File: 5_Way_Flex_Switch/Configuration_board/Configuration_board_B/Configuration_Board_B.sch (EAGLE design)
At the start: 4 parts

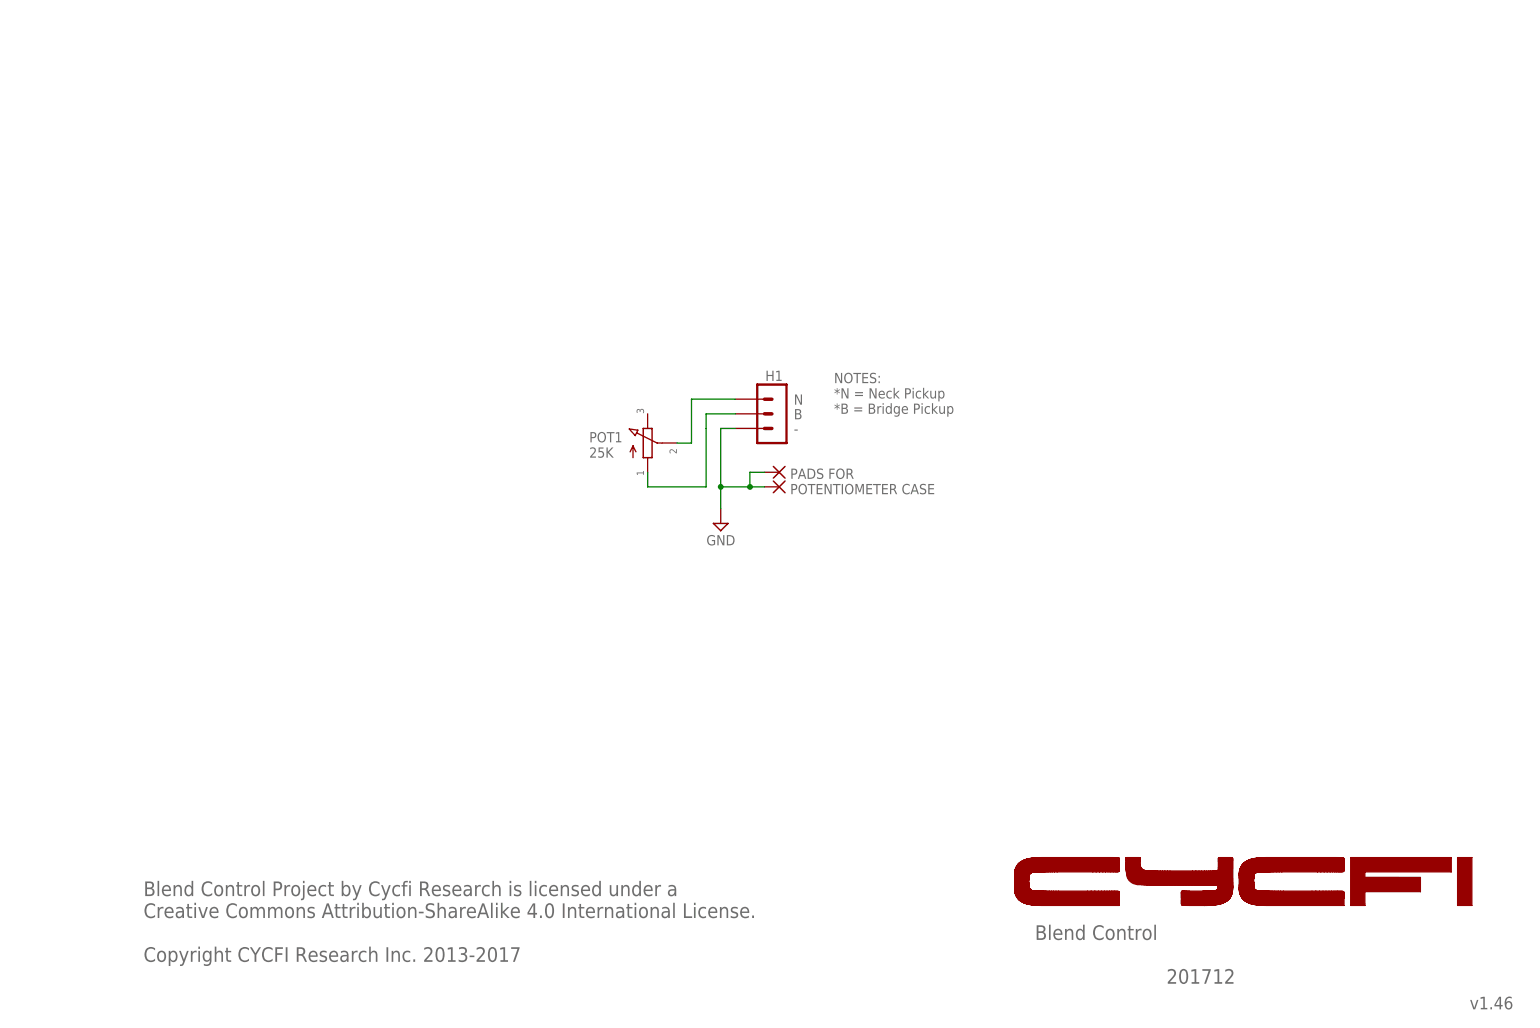
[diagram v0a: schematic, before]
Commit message: *organize 5-waay switch and its configuration board(a and b) *update license date *remove red frame schem pdf files, change with black frame *update document number
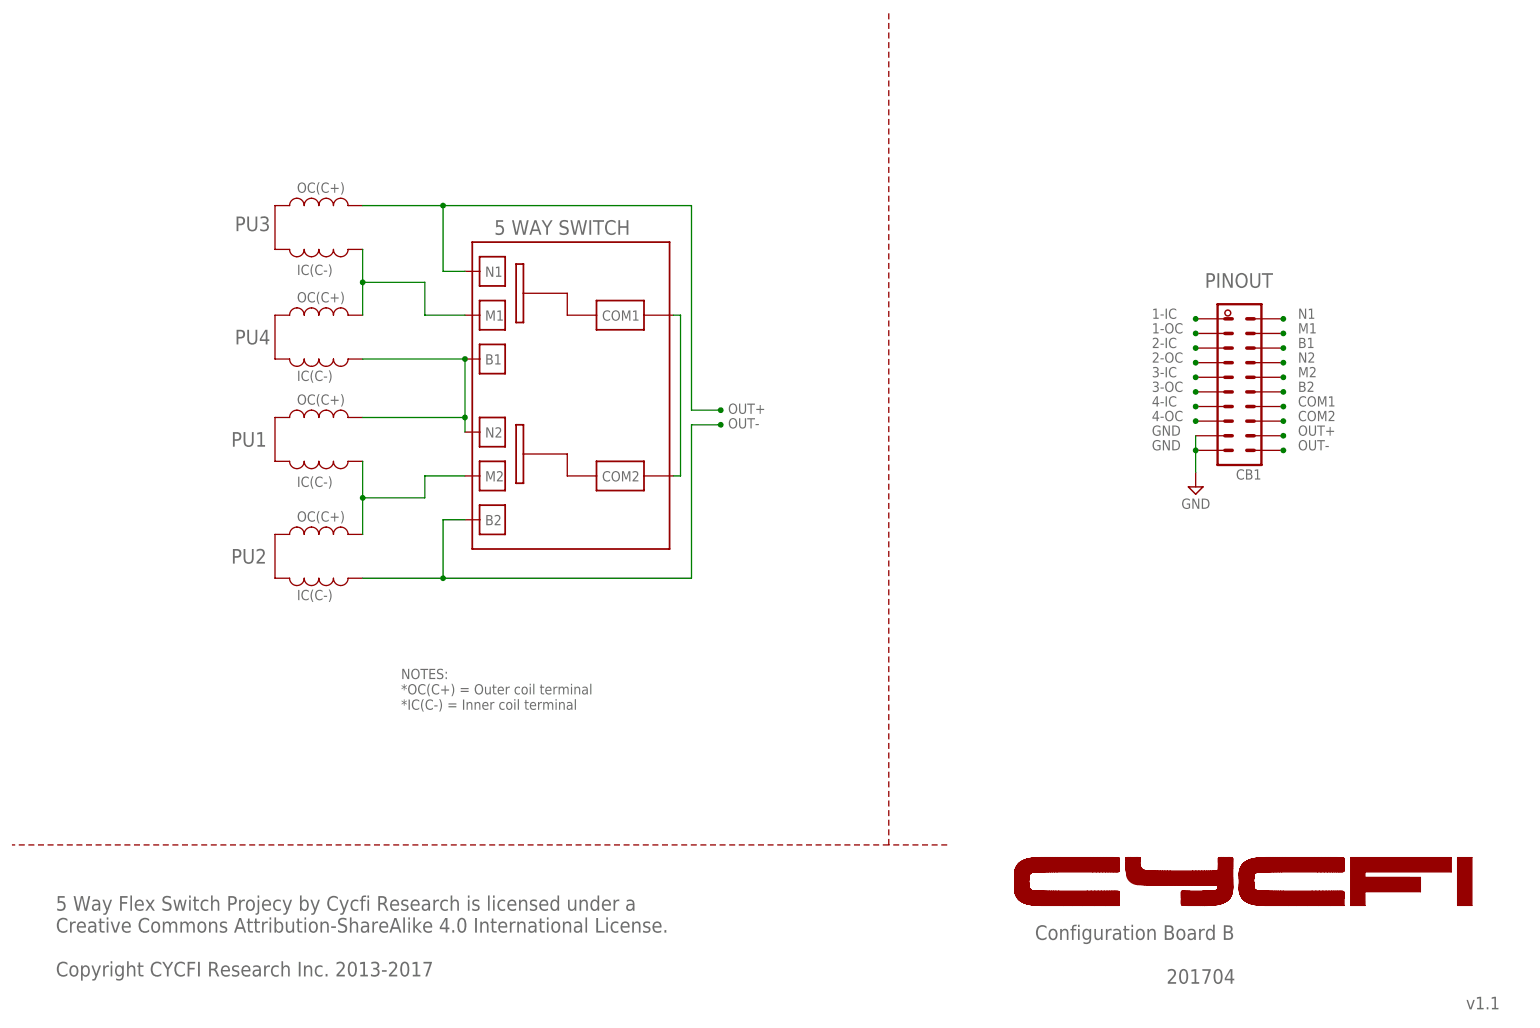
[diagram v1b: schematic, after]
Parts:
- removed GND3, GND4: (no value), wirepad:SMD2
- removed H1: 3PIN-SMD-2.54MM, CYCFI_Con:3PIN-SMD-2.54MM
- removed POT1: PDB181-GTR01, CYCFI_Passive:PDB181-GTR01
- added CB1: CONFIGURATION_BRD_CAST, CYCFI_Module_castellated:CONFIGURATION_BRD_CAST
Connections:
- removed net N$1: H1.3, POT1.2
- removed net N$3: H1.2, POT1.1
- new net 1: CB1.3-OC, CB1.N1, CB1.OUT+
- new net 2: CB1.3-IC, CB1.4-OC, CB1.M1
- new net 3: CB1.1-OC, CB1.4-IC, CB1.B1, CB1.N2
- new net 4: CB1.COM1, CB1.COM2
- new net 5: CB1.1-IC, CB1.2-OC, CB1.M2
- new net 6: CB1.2-IC, CB1.B2, CB1.OUT-
- net GND: now also CB1.GND, CB1.GND1; no longer GND3.P, GND4.P, H1.1
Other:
- note added: "1-IC"
- note added: "1-OC"
- note added: "2-IC"
- note added: "2-OC"
- note added: "201704"
- note added: "3-IC"
- note added: "3-OC"
- note added: "4-IC"
- note added: "4-OC"
- note added: "5 WAY SWITCH"
- note added: "5 Way Flex Switch Projecy by Cycfi Research is licensed under a Creative Commons Attribution-ShareAlike 4.0 International License. Copyright CYCFI Research Inc. 2013-2017"
- note added: "B1"
- note added: "B2"
- note added: "COM1"
- note added: "COM2"
- note added: "Configuration Board B"
- note added: "GND"
- note added: "IC(C-)"
- note added: "M1"
- note added: "M2"
- note added: "N1"
- note added: "N2"
- note added: "NOTES: *OC(C+) = Outer coil terminal *IC(C-) = Inner coil terminal"
- note added: "OC(C+)"
- note added: "OUT+"
- note added: "OUT-"
- note added: "PINOUT"
- note added: "PU1"
- note added: "PU2"
- note added: "PU3"
- note added: "PU4"
- note added: "v1.1"
- note removed: "-"
- note removed: "201712"
- note removed: "B"
- note removed: "Blend Control"
- note removed: "Blend Control Project by Cycfi Research is licensed under a Creative Commons Attribution-ShareAlike 4.0 International License. Copyright CYCFI Research Inc. 2013-2017"
- note removed: "N"
- note removed: "NOTES: *N = Neck Pickup *B = Bridge Pickup"
- note removed: "PADS FOR POTENTIOMETER CASE"
- note removed: "POT1 25K"
- note removed: "v1.46"

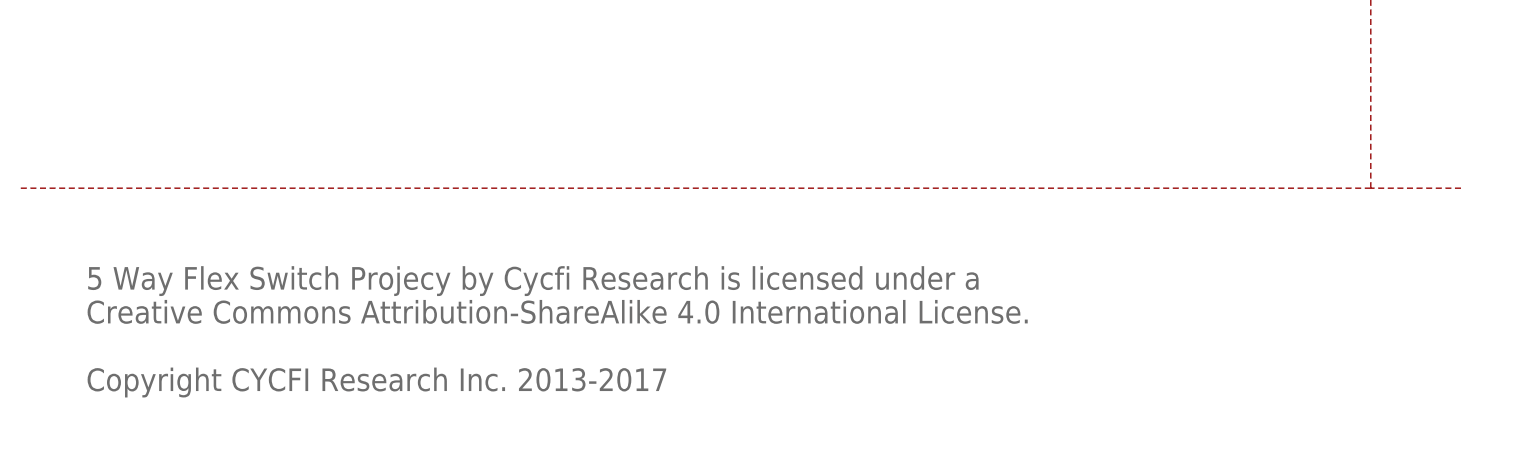
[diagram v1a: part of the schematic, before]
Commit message: Updated broken .sch files
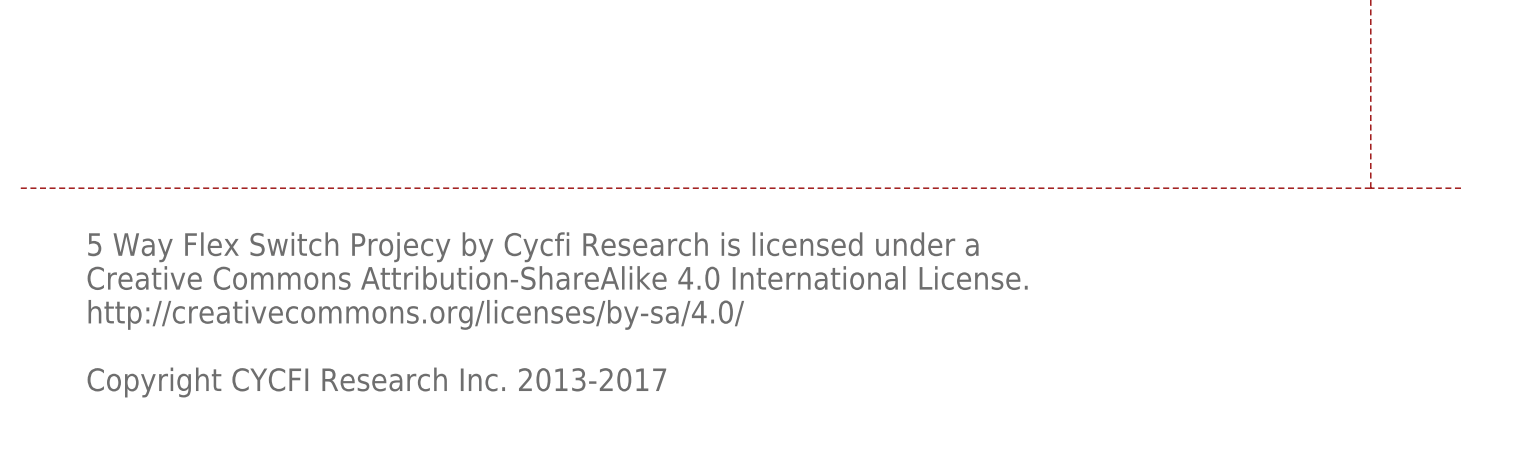
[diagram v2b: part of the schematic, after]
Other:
- note added: "5 Way Flex Switch Projecy by Cycfi Research is licensed under a Creative Commons Attribution-ShareAlike 4.0 International License. http://creativecommons.org/licenses/by-sa/4.0/ Copyright CYCFI Research Inc. 2013-2017"
- note removed: "5 Way Flex Switch Projecy by Cycfi Research is licensed under a Creative Commons Attribution-ShareAlike 4.0 International License. Copyright CYCFI Research Inc. 2013-2017"
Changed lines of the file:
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@@
 <text x="7.62" y="12.7" size="2.54" layer="95">5 Way Flex Switch Projecy by Cycfi Research is licensed under a
 Creative Commons Attribution-ShareAlike 4.0 International License.
+http://creativecommons.org/licenses/by-sa/4.0/
 Copyright CYCFI Research Inc. 2013-2017</text>
 <text x="200.66" y="11.43" size="2.54" layer="95">201704</text>
@@
 <instance part="FRAME1" gate="G$2" x="162.56" y="0" smashed="yes">
 <attribute name="LAST_DATE_TIME" x="175.26" y="1.27" size="2.54" layer="94" font="vector"/>
-<attribute name="SHEET" x="248.92" y="1.27" size="2.54" layer="94" font="vector"/>
+<attribute name="SHEET" x="248.92" y="1.27" size="2.54" layer="94"/>
 </instance>
 <instance part="SUPPLY3" gate="GND" x="205.74" y="97.79" smashed="yes" rot="MR0">
